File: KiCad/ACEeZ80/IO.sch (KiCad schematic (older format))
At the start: 8 parts, among them J2 Conn_02x06_Counter_Clockwise

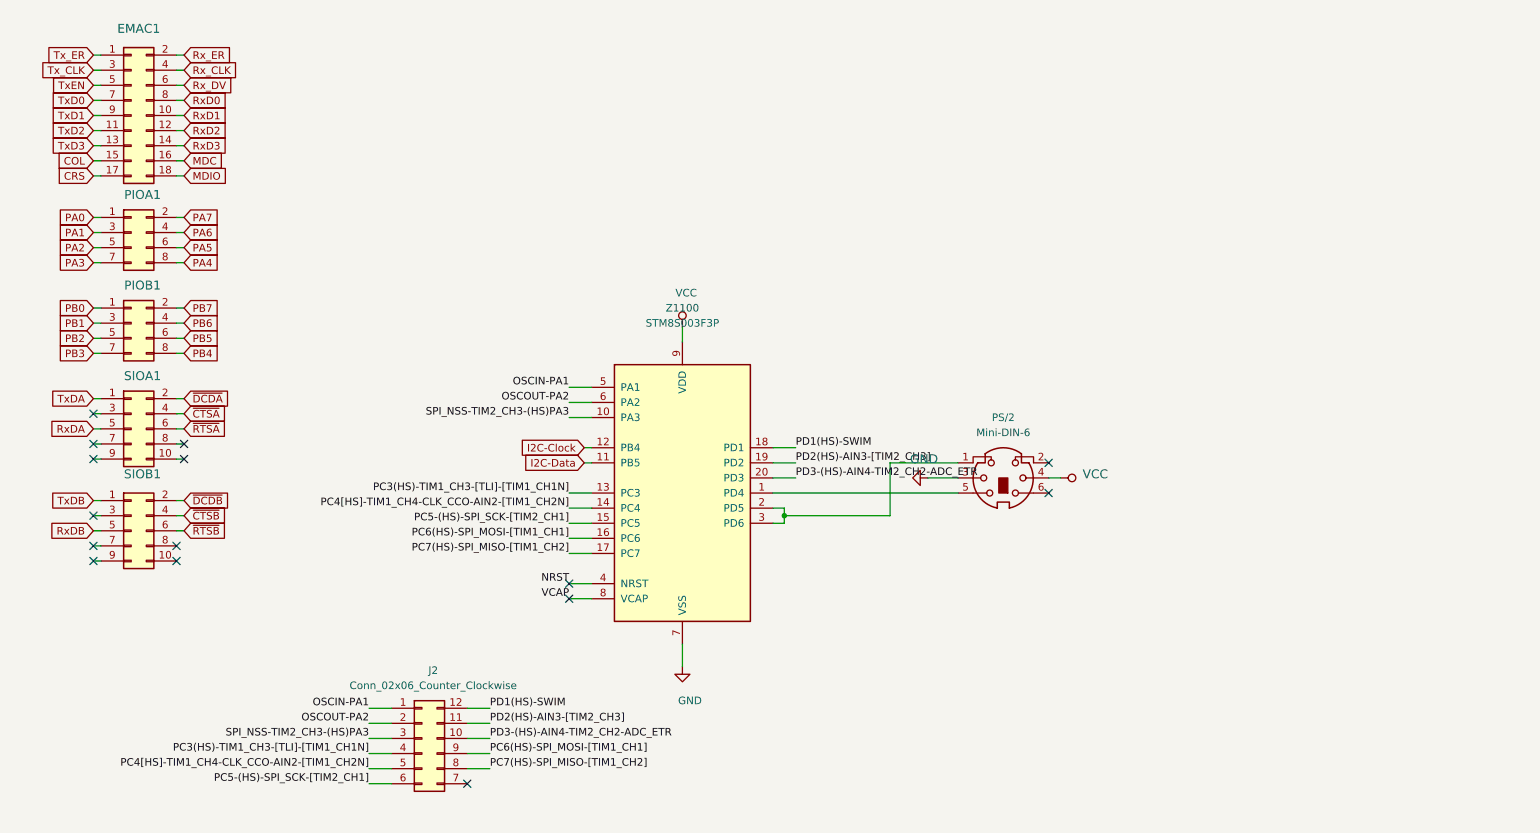
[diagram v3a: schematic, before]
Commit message: Improve EZ80,
Correct fault with layout of EdgeBoard. The test boards physically fitted old ACE add-ons but there was a mistake in the wiring.

Signed-off-by: John Bradley <flypie@rocketmail.com>
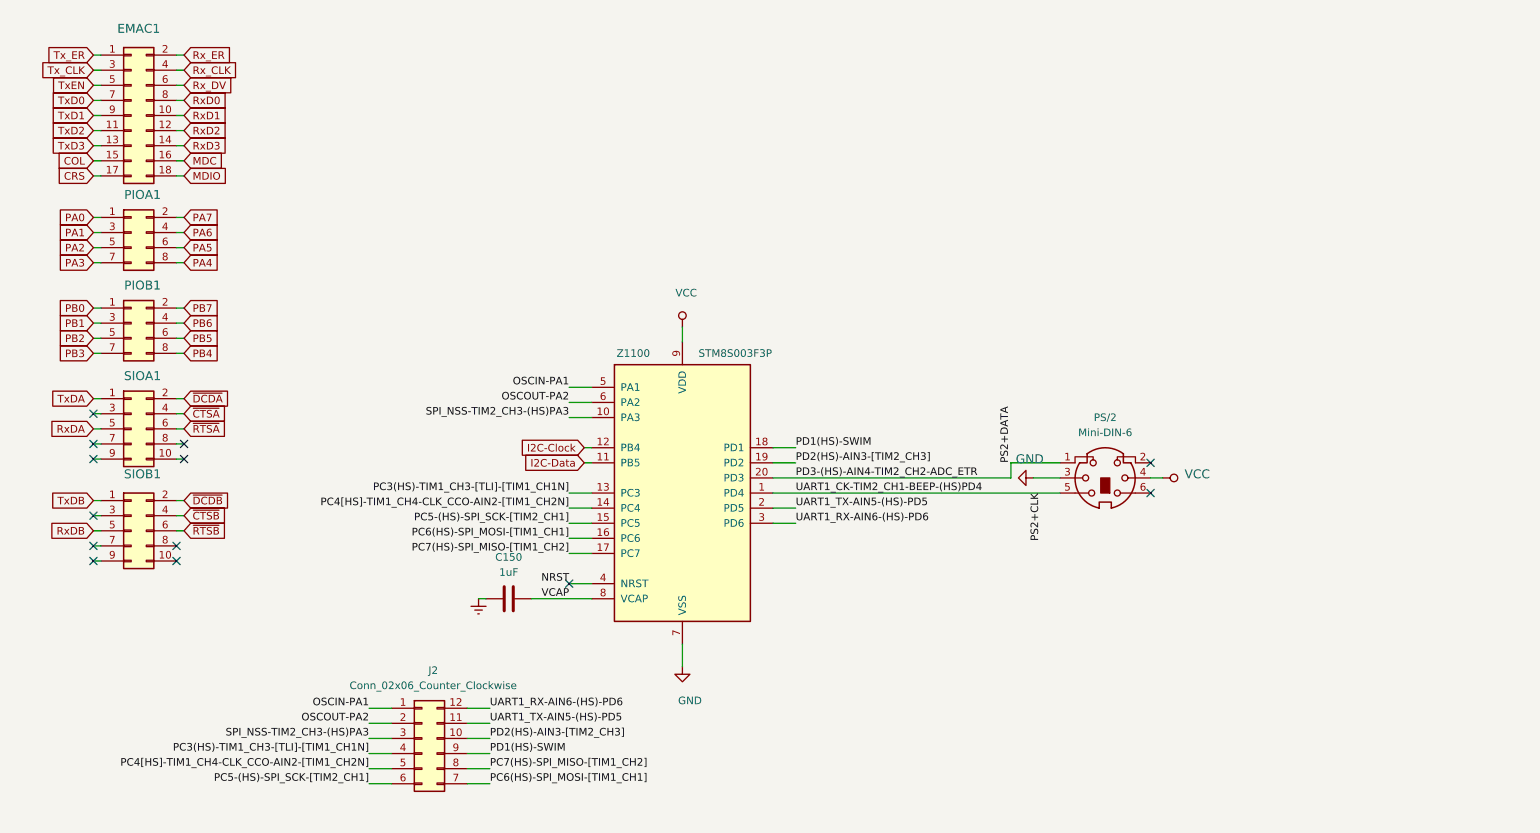
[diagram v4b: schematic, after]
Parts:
- added C150: 1uF, Capacitor_THT:C_Disc_D3.8mm_W2.6mm_P2.50mm, symbol Device:C
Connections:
- net PC6(HS)-SPI_MOSI-[TIM1_CH1]: now also J2.7 (Pin_7); no longer J2.9 (Pin_9)
- net PD1(HS)-SWIM: now also J2.9 (Pin_9); no longer J2.12 (Pin_12)
- net PD2(HS)-AIN3-[TIM2_CH3]: now also J2.10 (Pin_10); no longer J2.11 (Pin_11)
- net PD3-(HS)-AIN4-TIM2_CH2-ADC_ETR: now also PS/2.1; no longer J2.10 (Pin_10)
- net VCAP: now also C150.1
- net PS2+CLK: now reaches PS/2.5, Z1100.1 (PD4)
- new net Earth: C150.2
- new net UART1_RX-AIN6-(HS)-PD6: J2.12 (Pin_12), Z1100.3 (PD6)
- new net UART1_TX-AIN5-(HS)-PD5: J2.11 (Pin_11), Z1100.2 (PD5)
- no-connect marks 15 -> 13
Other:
- moved on the sheet: PS/2
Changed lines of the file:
@@
 L power:GND #~~~SUPPLY?
 U 1 1 618F6985
-P 6725 3475
+P 7425 3475
 AR Path="/618F6985" Ref="#~~~SUPPLY?"  Part="1"
 AR Path="/5D9DD1F0/618F6985" Ref="#~~~SUPPLY0103"  Part="1"
-F 0 "#~~~SUPPLY0103" H 6725 3475 50  0001 C CNN
-F 1 "GND" V 6600 3450 59  0000 C CNN
-F 2 "" H 6725 3475 50  0001 C CNN
-F 3 "" H 6725 3475 50  0001 C CNN
-	1    6725 3475
+F 0 "#~~~SUPPLY0103" H 7425 3475 50  0001 C CNN
+F 1 "GND" V 7300 3450 59  0000 C CNN
+F 2 "" H 7425 3475 50  0001 C CNN
+F 3 "" H 7425 3475 50  0001 C CNN
+	1    7425 3475
 	0    1    1    0
 $EndComp
 Wire Wire Line
-	6925 3475 6725 3475
-Wire Wire Line
-	7605 3475 7525 3475
-NoConn ~ 7525 3575
-NoConn ~ 7525 3375
+	7600 3475 7425 3475
+Wire Wire Line
+	8280 3475 8200 3475
+NoConn ~ 8200 3575
+NoConn ~ 8200 3375
 $Comp
 L Connector:Mini-DIN-6 PS/2
 U 1 1 618F6975
-P 7225 3475
+P 7900 3475
 AR Path="/5D9DD1F0/618F6975" Ref="PS/2"  Part="1"
 AR Path="/618F6975" Ref="J?"  Part="1"
-F 0 "PS/2" H 7225 3075 50  0000 C CNN
-F 1 "Mini-DIN-6" H 7225 3175 50  0000 C CNN
-F 2 "Local:5749180-1" H 7225 3475 50  0001 C CNN
-F 3 "http://service.powerdynamics.com/ec/Catalog17/Section%2011.pdf" H 7225 3475 50  0001 C CNN
-	1    7225 3475
+F 0 "PS/2" H 7900 3075 50  0000 C CNN
+F 1 "Mini-DIN-6" H 7900 3175 50  0000 C CNN
+F 2 "Local:5749180-1" H 7900 3475 50  0001 C CNN
+F 3 "http://service.powerdynamics.com/ec/Catalog17/Section%2011.pdf" H 7900 3475 50  0001 C CNN
+	1    7900 3475
 	-1   0    0    1
 $EndComp
@@
 U 1 1 5DC55916
 P 5100 3575
-F 0 "Z1100" H 5100 4800 50  0000 C CNN
-F 1 "STM8S003F3P" H 5100 4700 50  0000 C CNN
+F 0 "Z1100" H 4775 4500 50  0000 C CNN
+F 1 "STM8S003F3P" H 5450 4500 50  0000 C CNN
 F 2 "Package_SO:TSSOP-20_4.4x6.5mm_P0.65mm" H 5150 4675 50  0001 L CNN
 F 3 "http://www.st.com/st-web-ui/static/active/en/resource/technical/document/datasheet/DM00024550.pdf" H 5050 3175 50  0001 C CNN
@@
 	1    0    0    -1
 $EndComp
-Wire Wire Line
-	5700 3575 6925 3575
 $Comp
 L power:VCC #~~~P+?
 U 1 1 618F697D
-P 7605 3475
+P 8280 3475
 AR Path="/618F697D" Ref="#~~~P+?"  Part="1"
 AR Path="/5D9DD1F0/618F697D" Ref="#~~~P+0101"  Part="1"
-F 0 "#~~~P+0101" H 7605 3475 50  0001 C CNN
-F 1 "VCC" V 7630 3620 59  0000 L CNN
-F 2 "" H 7605 3475 50  0001 C CNN
-F 3 "" H 7605 3475 50  0001 C CNN
-	1    7605 3475
+F 0 "#~~~P+0101" H 8280 3475 50  0001 C CNN
+F 1 "VCC" V 8305 3620 59  0000 L CNN
+F 2 "" H 8280 3475 50  0001 C CNN
+F 3 "" H 8280 3475 50  0001 C CNN
+	1    8280 3475
 	0    1    -1   0
 $EndComp
 Wire Wire Line
-	6925 3375 6475 3375
-Wire Wire Line
-	6475 3375 6475 3725
-Wire Wire Line
-	6475 3725 5775 3725
-Wire Wire Line
-	5775 3725 5775 3675
-Wire Wire Line
-	5775 3675 5700 3675
-Wire Wire Line
-	5700 3775 5775 3775
-Wire Wire Line
-	5775 3775 5775 3725
-Connection ~ 5775 3725
+	7600 3375 7275 3375
 Wire Wire Line
 	5100 4575 5100 4725
@@
 	4500 3375 4450 3375
 Wire Wire Line
-	4500 2875 4350 2875
-Text Label 4350 2875 2    50   ~ 0
-OSCIN-PA1
-Wire Wire Line
 	4500 2975 4350 2975
 Text Label 4350 2975 2    50   ~ 0
@@
 NRST
 Wire Wire Line
-	4500 4275 4350 4275
+	4500 4275 4100 4275
 Text Label 4350 4275 2    50   ~ 0
 VCAP
-Wire Wire Line
-	5700 3275 5850 3275
 Text Label 5850 3275 0    50   ~ 0
 PD1(HS)-SWIM
@@
 Text Label 5850 3375 0    50   ~ 0
 PD2(HS)-AIN3-[TIM2_CH3]
-Wire Wire Line
-	5700 3475 5850 3475
 Text Label 5850 3475 0    50   ~ 0
 PD3-(HS)-AIN4-TIM2_CH2-ADC_ETR
@@
 $EndComp
 Wire Wire Line
-	3175 5000 3025 5000
-Text Label 3025 5000 2    50   ~ 0
-OSCIN-PA1
-Wire Wire Line
 	3175 5100 3025 5100
 Text Label 3025 5100 2    50   ~ 0
 OSCOUT-PA2
-Wire Wire Line
-	3175 5200 3025 5200
 Text Label 3025 5200 2    50   ~ 0
 SPI_NSS-TIM2_CH3-(HS)PA3
 Wire Wire Line
-	3675 5000 3825 5000
-Text Label 3825 5000 0    50   ~ 0
+	3675 5300 3825 5300
+Text Label 3825 5300 0    50   ~ 0
 PD1(HS)-SWIM
-Wire Wire Line
-	3675 5100 3825 5100
-Text Label 3825 5100 0    50   ~ 0
-PD2(HS)-AIN3-[TIM2_CH3]
 Wire Wire Line
 	3675 5200 3825 5200
 Text Label 3825 5200 0    50   ~ 0
-PD3-(HS)-AIN4-TIM2_CH2-ADC_ETR
+PD2(HS)-AIN3-[TIM2_CH3]
 Wire Wire Line
 	3175 5300 3025 5300
@@
 PC7(HS)-SPI_MISO-[TIM1_CH2]
 Wire Wire Line
-	3675 5300 3825 5300
-Text Label 3825 5300 0    50   ~ 0
+	3675 5500 3825 5500
+Text Label 3825 5500 0    50   ~ 0
 PC6(HS)-SPI_MOSI-[TIM1_CH1]
-NoConn ~ 4350 4275
 NoConn ~ 4350 4175
-NoConn ~ 3675 5500
+Wire Wire Line
+	4350 2875 4500 2875
+Wire Wire Line
+	5700 3575 7600 3575
+Wire Wire Line
+	5850 3275 5700 3275
+Wire Wire Line
+	5700 3675 5850 3675
+Wire Wire Line
+	5700 3775 5850 3775
+Text Label 5850 3675 0    50   ~ 0
+UART1_TX-AIN5-(HS)-PD5
+Text Label 5850 3775 0    50   ~ 0
+UART1_RX-AIN6-(HS)-PD6
+Wire Wire Line
+	3675 5100 3825 5100
+Wire Wire Line
+	3675 5000 3825 5000
+Text Label 3825 5100 0    50   ~ 0
+UART1_TX-AIN5-(HS)-PD5
+Text Label 3825 5000 0    50   ~ 0
+UART1_RX-AIN6-(HS)-PD6
+$Comp
+L Device:C C150
+U 1 1 5DE2B980
+P 3950 4275
+F 0 "C150" V 3675 4275 50  0000 C CNN
+F 1 "1uF" V 3775 4275 50  0000 C CNN
+F 2 "Capacitor_THT:C_Disc_D3.8mm_W2.6mm_P2.50mm" H 3988 4125 50  0001 C CNN
+F 3 "~" H 3950 4275 50  0001 C CNN
+	1    3950 4275
+	0    1    1    0
+$EndComp
+Wire Wire Line
+	3800 4275 3750 4275
+$Comp
+L power:Earth #PWR0104
+U 1 1 5DE2FDCB
+P 3750 4275
+F 0 "#PWR0104" H 3750 4025 50  0001 C CNN
+F 1 "Earth" H 3750 4125 50  0001 C CNN
+F 2 "" H 3750 4275 50  0001 C CNN
+F 3 "~" H 3750 4275 50  0001 C CNN
+	1    3750 4275
+	1    0    0    -1
+$EndComp
+Text Label 5850 3575 0    50   ~ 0
+UART1_CK-TIM2_CH1-BEEP-(HS)PD4
+Text Label 4350 2875 2    50   ~ 0
+OSCIN-PA1
+Text Label 7275 3375 1    50   ~ 0
+PS2+DATA
+Text Label 7475 3575 3    50   ~ 0
+PS2+CLK
+Wire Wire Line
+	7275 3475 7275 3375
+Wire Wire Line
+	5700 3475 7275 3475
+Wire Wire Line
+	3025 5000 3175 5000
+Text Label 3025 5000 2    50   ~ 0
+OSCIN-PA1
+Wire Wire Line
+	3025 5200 3175 5200
 $EndSCHEMATC

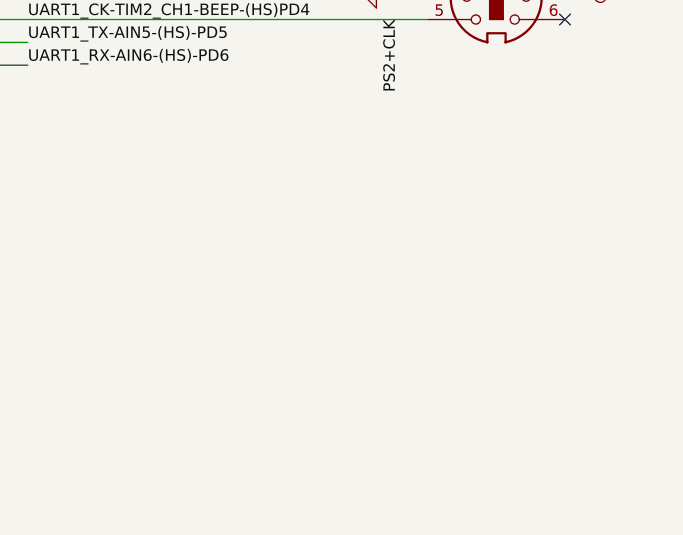
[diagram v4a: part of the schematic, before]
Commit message: Layout updates. STart STM8 code for PS/2 decode.
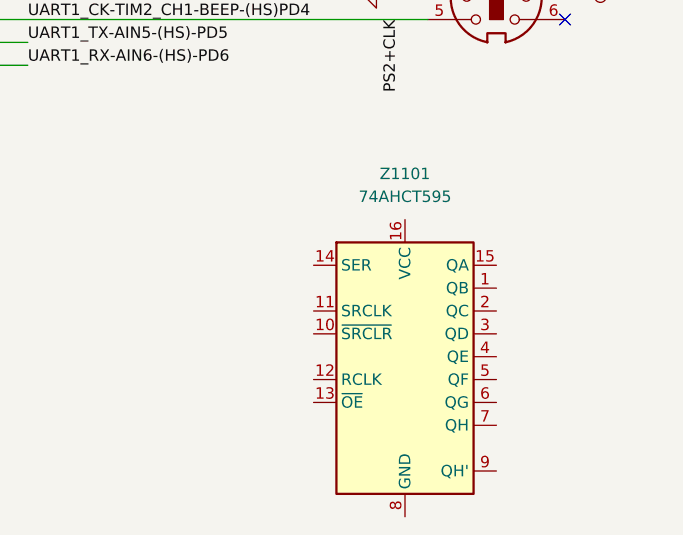
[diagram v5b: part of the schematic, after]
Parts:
- added Z1101: 74AHCT595, Package_DIP:DIP-16_W7.62mm, symbol 74xx:74HCT595
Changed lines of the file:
@@
 EESchema Schematic File Version 4
-LIBS:ACEeZ80-cache
 EELAYER 30 0
 EELAYER END
@@
 Wire Wire Line
 	3025 5200 3175 5200
+$Comp
+L 74xx:74HCT595 Z1101
+U 1 1 5DF324BE
+P 7500 5050
+F 0 "Z1101" H 7500 5850 50  0000 C CNN
+F 1 "74AHCT595" H 7500 5750 50  0000 C CNN
+F 2 "Package_DIP:DIP-16_W7.62mm" H 7500 5050 50  0001 C CNN
+F 3 "http://www.ti.com/lit/ds/symlink/sn74ahct595.pdf" H 7500 5050 50  0001 C CNN
+	1    7500 5050
+	1    0    0    -1
+$EndComp
 $EndSCHEMATC

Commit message: Update ACE3NOKB to reflect errors in Mem Decode. ACE5NOKB test SMT ideas. Added 180 & 380.
Signed-off-by: John Bradley <flypie@rocketmail.com>
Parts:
- renumbered PIOA1 to PIOA?, PIOB1 to PIOB?, EMAC1 to SIOA?, SIOA1 to SIOA?, SIOB1 to SIOB?
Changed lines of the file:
@@
 U 1 1 618F6985
 P 7425 3475
-AR Path="/618F6985" Ref="#~~~SUPPLY?"  Part="1"
-AR Path="/5D9DD1F0/618F6985" Ref="#~~~SUPPLY0103"  Part="1"
 F 0 "#~~~SUPPLY0103" H 7425 3475 50  0001 C CNN
 F 1 "GND" V 7300 3450 59  0000 C CNN
@@
 U 1 1 618F6975
 P 7900 3475
-AR Path="/5D9DD1F0/618F6975" Ref="PS/2"  Part="1"
-AR Path="/618F6975" Ref="J?"  Part="1"
 F 0 "PS/2" H 7900 3075 50  0000 C CNN
 F 1 "Mini-DIN-6" H 7900 3175 50  0000 C CNN
@@
 U 1 1 5ED93C32
 P 1450 1075
-AR Path="/5ED93C32" Ref="SIOA?"  Part="1"
-AR Path="/5D9DD1F0/5ED93C32" Ref="EMAC1"  Part="1"
 F 0 "EMAC1" H 1500 1650 59  0000 C CNN
 F 1 "2510-" H 1300 1180 59  0001 L BNN
@@
 U 1 1 6187201B
 P 1450 3150
-AR Path="/6187201B" Ref="SIOA?"  Part="1"
-AR Path="/5D9DD1F0/6187201B" Ref="SIOA1"  Part="1"
 F 0 "SIOA1" H 1525 3500 59  0000 C CNN
 F 1 "2510-" H 1300 3255 59  0001 L BNN
@@
 U 1 1 61872035
 P 1450 3825
-AR Path="/61872035" Ref="SIOB?"  Part="1"
-AR Path="/5D9DD1F0/61872035" Ref="SIOB1"  Part="1"
 F 0 "SIOB1" H 1525 4200 59  0000 C CNN
 F 1 "2510-" H 1300 3930 59  0001 L BNN
@@
 U 1 1 61872040
 P 1450 2450
-AR Path="/61872040" Ref="PIOB?"  Part="1"
-AR Path="/5D9DD1F0/61872040" Ref="PIOB1"  Part="1"
 F 0 "PIOB1" H 1525 2700 59  0000 C CNN
 F 1 "2510-" H 1300 2555 59  0001 L BNN
@@
 U 1 1 61871FF8
 P 1450 1850
-AR Path="/61871FF8" Ref="PIOA?"  Part="1"
-AR Path="/5D9DD1F0/61871FF8" Ref="PIOA1"  Part="1"
 F 0 "PIOA1" H 1525 2100 59  0000 C CNN
 F 1 "2510-" H 1300 1955 59  0001 L BNN
@@
 U 1 1 618F697D
 P 8280 3475
-AR Path="/618F697D" Ref="#~~~P+?"  Part="1"
-AR Path="/5D9DD1F0/618F697D" Ref="#~~~P+0101"  Part="1"
 F 0 "#~~~P+0101" H 8280 3475 50  0001 C CNN
 F 1 "VCC" V 8305 3620 59  0000 L CNN
